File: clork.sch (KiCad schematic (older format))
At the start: 29 parts, among them J1 UE27AC54100, J2 USB_B_Micro, M1 Stepper_Motor_unipolar_5pin, U1 RT9193-33GB, U2 STM32F103C8Tx, U3 ULN2003, Y1 8 Mhz, Y2 32.768 kHz

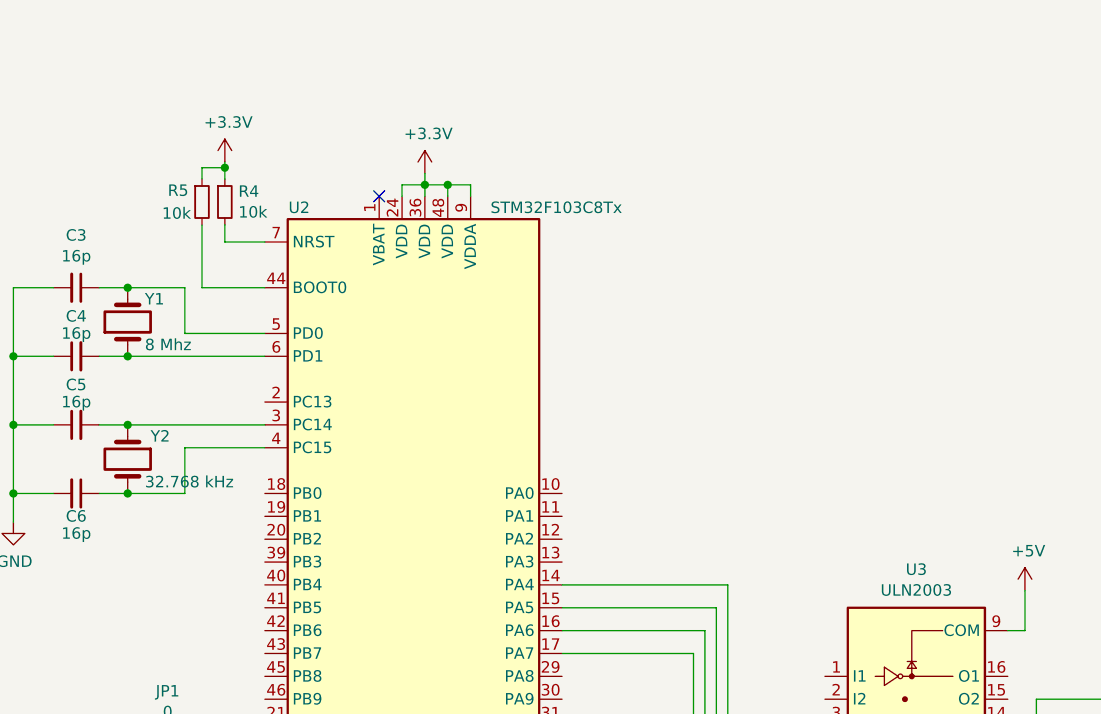
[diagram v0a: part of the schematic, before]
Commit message: Fixed PD resistors for BOOT0 and BOOT1
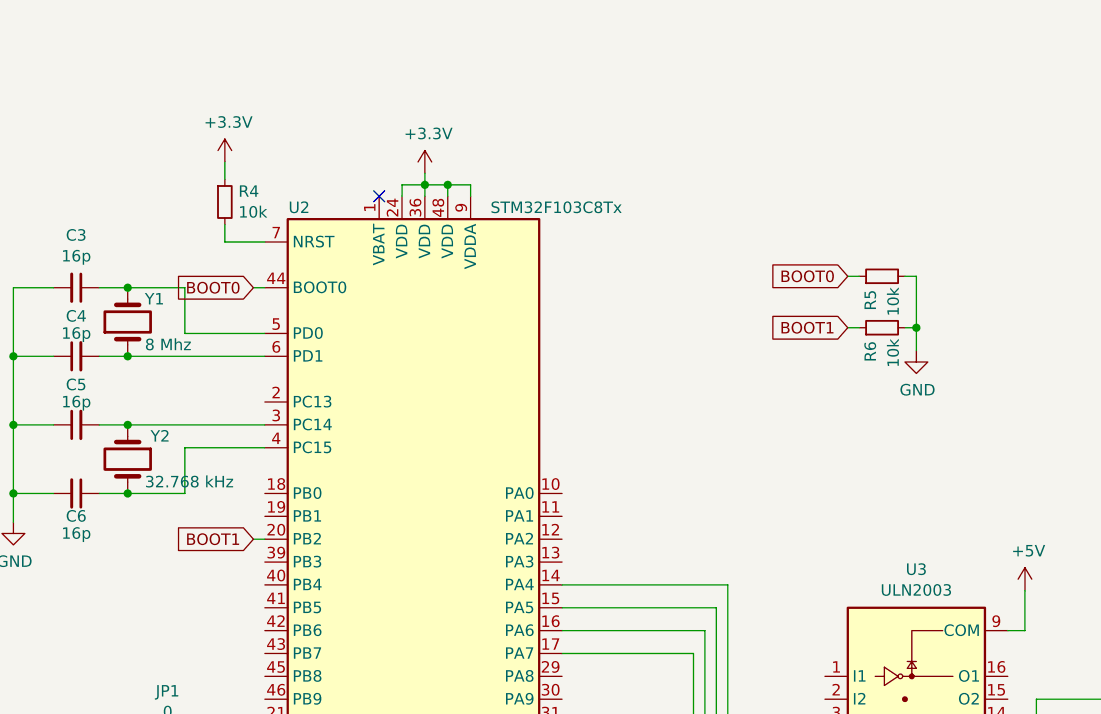
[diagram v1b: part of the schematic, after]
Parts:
- added R6: 10k, Resistor_SMD:R_0603_1608Metric, symbol Device:R_Small
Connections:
- net +3V3: no longer R5.1
- net GND: now also R5.2, R6.2
- net BOOT1: now reaches U2.20 (PB2)
- net BOOT1: now also R6.1
- net BOOT0: now reaches U2.44 (BOOT0)
- net BOOT0: now also R5.1; no longer R5.2
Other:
- moved on the sheet: R5
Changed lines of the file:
@@
 EESchema Schematic File Version 4
+LIBS:clork-cache
 EELAYER 29 0
 EELAYER END
@@
 $EndComp
 Wire Wire Line
-	4775 2325 4775 2350
-Wire Wire Line
 	4775 2600 4775 2675
 Wire Wire Line
@@
 L Device:R_Small R5
 U 1 1 5E36936F
-P 4675 2500
-F 0 "R5" H 4525 2550 50  0000 L CNN
-F 1 "10k" H 4500 2450 50  0000 L CNN
-F 2 "Resistor_SMD:R_0603_1608Metric" H 4675 2500 50  0001 C CNN
-F 3 "~" H 4675 2500 50  0001 C CNN
-	1    4675 2500
-	1    0    0    -1
-$EndComp
-Wire Wire Line
-	4675 2875 4675 2600
-Wire Wire Line
-	4675 2875 4950 2875
-Wire Wire Line
-	4675 2350 4775 2350
-Connection ~ 4775 2350
-Wire Wire Line
-	4775 2350 4775 2400
-Wire Wire Line
-	4675 2350 4675 2400
+P 7650 2825
+F 0 "R5" H 7500 2875 50  0000 L CNN
+F 1 "10k" H 7475 2775 50  0000 L CNN
+F 2 "Resistor_SMD:R_0603_1608Metric" H 7650 2825 50  0001 C CNN
+F 3 "~" H 7650 2825 50  0001 C CNN
+	1    7650 2825
+	0    -1   -1   0
+$EndComp
 $Comp
 L Device:Jumper_NO_Small JP1
@@
 	1    0    0    -1
 $EndComp
+Wire Wire Line
+	4775 2325 4775 2400
+$Comp
+L power:GND #PWR0117
+U 1 1 5E1447F7
+P 7800 3150
+F 0 "#PWR0117" H 7800 2900 50  0001 C CNN
+F 1 "GND" H 7805 2977 50  0000 C CNN
+F 2 "" H 7800 3150 50  0001 C CNN
+F 3 "" H 7800 3150 50  0001 C CNN
+	1    7800 3150
+	1    0    0    -1
+$EndComp
+$Comp
+L Device:R_Small R6
+U 1 1 5E14541A
+P 7650 3050
+F 0 "R6" H 7500 3100 50  0000 L CNN
+F 1 "10k" H 7475 3000 50  0000 L CNN
+F 2 "Resistor_SMD:R_0603_1608Metric" H 7650 3050 50  0001 C CNN
+F 3 "~" H 7650 3050 50  0001 C CNN
+	1    7650 3050
+	0    -1   -1   0
+$EndComp
+Wire Wire Line
+	7750 2825 7800 2825
+Wire Wire Line
+	7800 2825 7800 3050
+Wire Wire Line
+	7750 3050 7800 3050
+Connection ~ 7800 3050
+Wire Wire Line
+	7800 3050 7800 3150
+Text GLabel 7500 2825 0    50   Input ~ 0
+BOOT0
+Text GLabel 7500 3050 0    50   Input ~ 0
+BOOT1
+Wire Wire Line
+	7500 2825 7550 2825
+Wire Wire Line
+	7550 3050 7500 3050
+Text GLabel 4900 2875 0    50   Input ~ 0
+BOOT0
+Wire Wire Line
+	4900 2875 4950 2875
+Text GLabel 4900 3975 0    50   Input ~ 0
+BOOT1
+Wire Wire Line
+	4900 3975 4950 3975
 $EndSCHEMATC

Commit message: Added button for setting time
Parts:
- added SW1: SW_Push, Button_Switch_SMD:SW_SPST_PTS645, symbol Switch:SW_Push
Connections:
- net GND: now also SW1.1
- net at U2.22 (PB11): now also SW1.2
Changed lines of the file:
@@
 Wire Wire Line
 	4900 3975 4950 3975
+$Comp
+L power:GND #PWR0122
+U 1 1 5E173C7B
+P 3550 4975
+F 0 "#PWR0122" H 3550 4725 50  0001 C CNN
+F 1 "GND" H 3555 4802 50  0000 C CNN
+F 2 "" H 3550 4975 50  0001 C CNN
+F 3 "" H 3550 4975 50  0001 C CNN
+	1    3550 4975
+	1    0    0    -1
+$EndComp
+Wire Wire Line
+	3600 4600 3550 4600
+Wire Wire Line
+	4000 4600 4875 4600
+Wire Wire Line
+	4875 4600 4875 4875
+Wire Wire Line
+	4875 4875 4950 4875
+$Comp
+L Switch:SW_Push SW1
+U 1 1 5E194542
+P 3800 4600
+F 0 "SW1" H 3800 4885 50  0000 C CNN
+F 1 "SW_Push" H 3800 4794 50  0000 C CNN
+F 2 "Button_Switch_SMD:SW_SPST_PTS645" H 3800 4800 50  0001 C CNN
+F 3 "" H 3800 4800 50  0001 C CNN
+	1    3800 4600
+	1    0    0    -1
+$EndComp
+Wire Wire Line
+	3550 4600 3550 4975
 $EndSCHEMATC

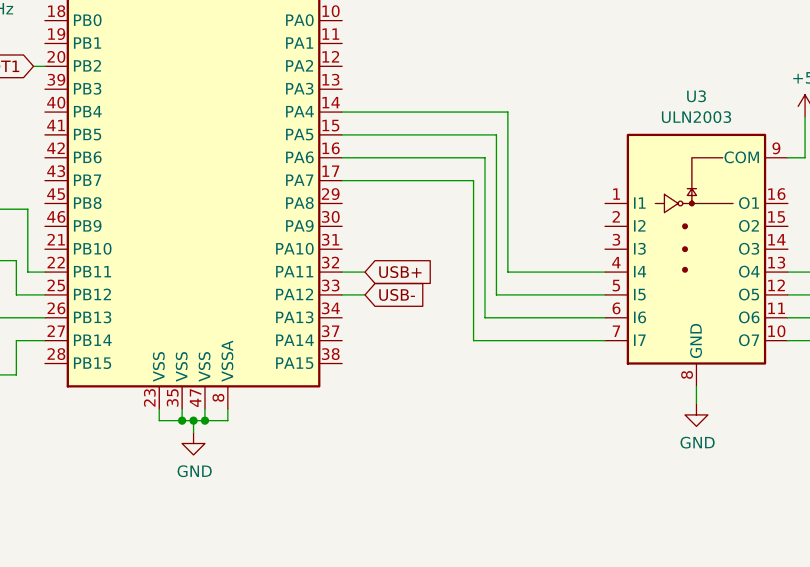
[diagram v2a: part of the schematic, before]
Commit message: Fixed reversed USB + and -
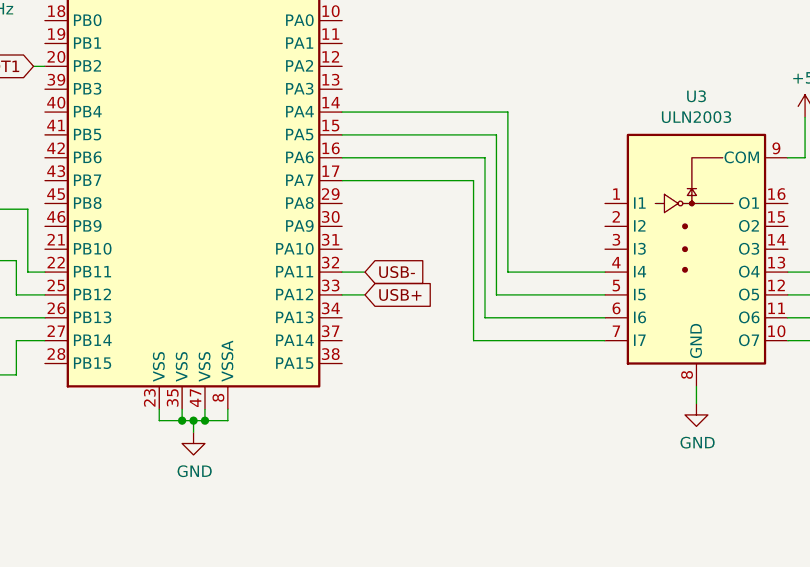
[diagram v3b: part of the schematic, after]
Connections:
- net USB+: now also U2.33 (PA12); no longer U2.32 (PA11)
- net USB-: now also U2.32 (PA11); no longer U2.33 (PA12)
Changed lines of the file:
@@
 Wire Wire Line
 	3225 6500 3750 6500
+Text GLabel 6350 4975 2    50   Input ~ 0
+USB+
 Text GLabel 6350 4875 2    50   Input ~ 0
-USB+
-Text GLabel 6350 4975 2    50   Input ~ 0
 USB-
 Wire Wire Line
